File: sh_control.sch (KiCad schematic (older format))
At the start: 77 parts, among them IC1 SN75240PW, IC2 LM317MDCY, IC3 TPS73533DRBT, IC4 TLV76733DGNR, IC5 TUSB2046IBVF, IC6 TPS2044BDR, IC7 SN75240PW, J1 USB_B_Micro, J2 10129381-906001BLF, J3 10129381-906001BLF, J4 USB_A, J5 USB_A, Y1 6MHz

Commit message: finished schematic, placing parts and so on
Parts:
- added C27, C28, C29, C30: 22pF, storage:C_22pF, symbol Device:C_Small
- added C31, C32: 100uF, storage:C_100uF, symbol Device:CP_Small
- added PortC1, PortD1: USB_A, Connector_USB:USB_A_Molex_67643_Horizontal, symbol Connector:USB_A
- added R27, R28, R29, R30: 15k, storage:R_15K, symbol Device:R_Small
- R14, R15, R16, R17: value 15k -> 22; footprint storage:R_15K -> storage:R_22
- renumbered D3 to Buck_1, D4 to Buck_2, TP1 to GND1, D5 to LDO1, J4 to PortA1, J5 to PortB1, TP2 to VBUS1
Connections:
- net DM3: now also R14.2, C27.1; no longer R15.2
- net DM4: now also C28.1
- net DP3: now also R15.2, C29.1; no longer R14.2
- net DP4: now also C30.1
- net GND: now also C27.2, C28.2, C29.2, C30.2, C31.2, C32.2, PortC1.4 (GND), PortC1.5 (Shield), PortD1.4 (GND), R27.1, R28.1, R29.1, R30.1; no longer R14.1, R15.1, R16.1, R17.1
- net OUT4: now reaches IC6.10 (OUT4)
- net OUT4: now also C32.1, PortD1.1 (VBUS)
- net OUT3: now reaches IC6.11 (OUT3)
- net OUT3: now also C31.1, PortC1.1 (VBUS)
- new net DM_downstream3: PortC1.2 (D-), R14.1, R29.2
- new net DM_downstream4: PortD1.2 (D-), R16.1, R30.2
- new net DP_downstream3: PortC1.3 (D+), R15.1, R27.2
- new net DP_downstream4: PortD1.3 (D+), R17.1, R28.2
- no-connect marks 12 -> 10
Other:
- moved on the sheet: C14, C15, C16, C17, C18, C21, C22, C23, C24, C25, C26, IC5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

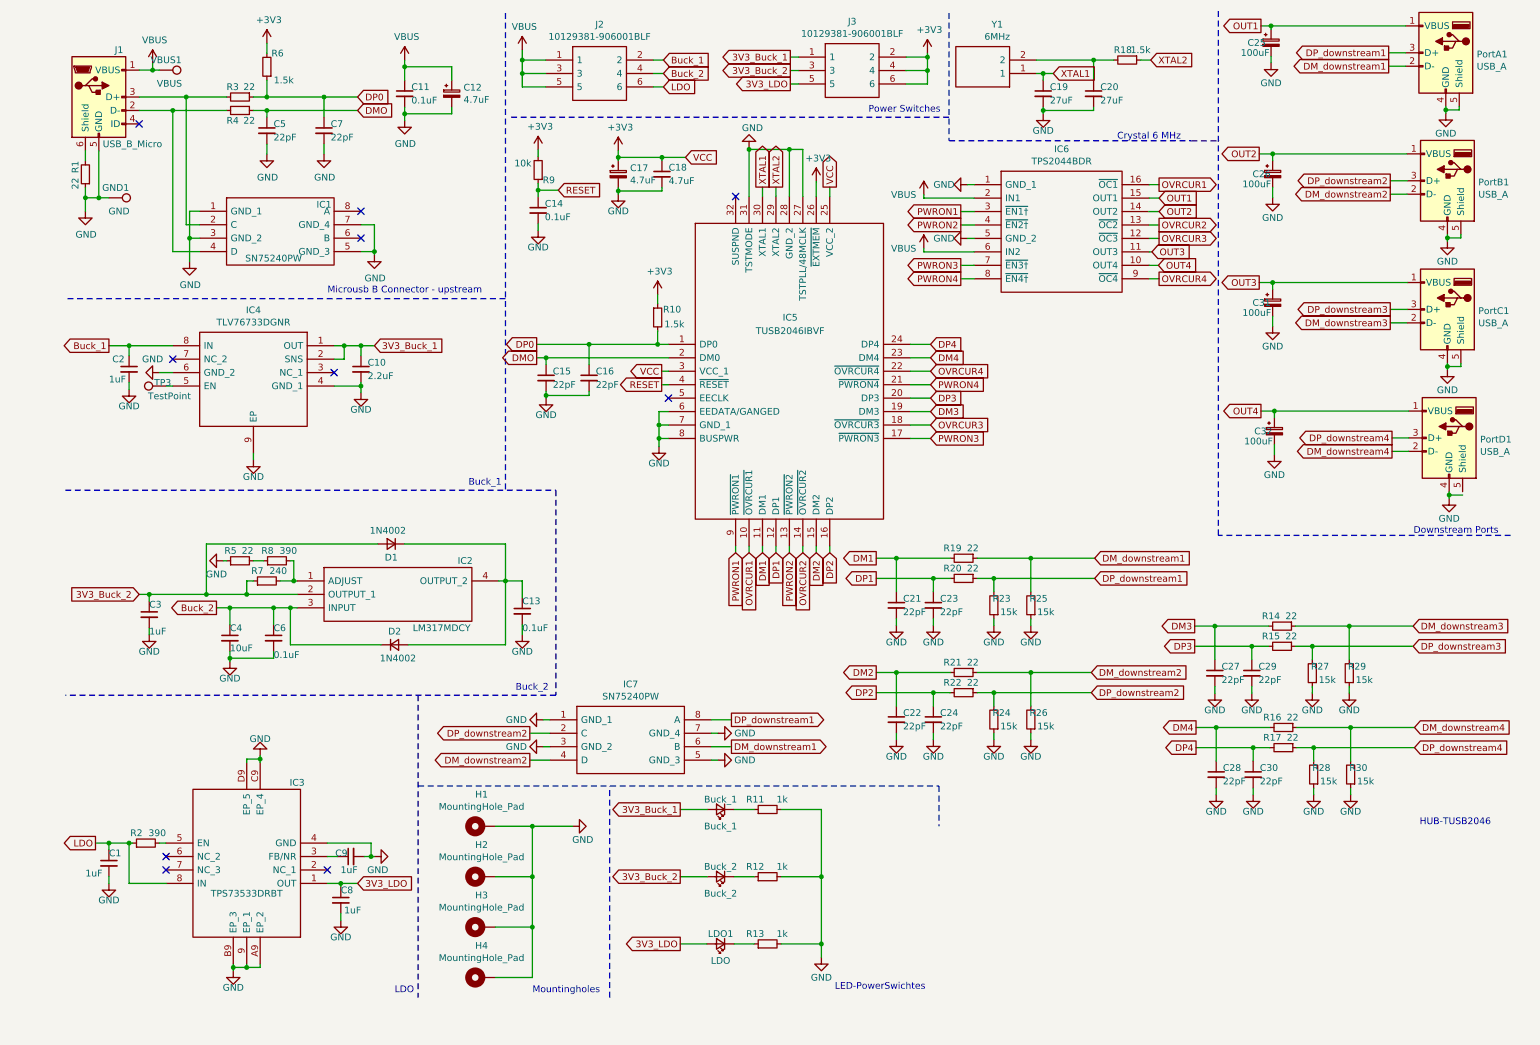
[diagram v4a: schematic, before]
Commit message: finished hub, added reste button
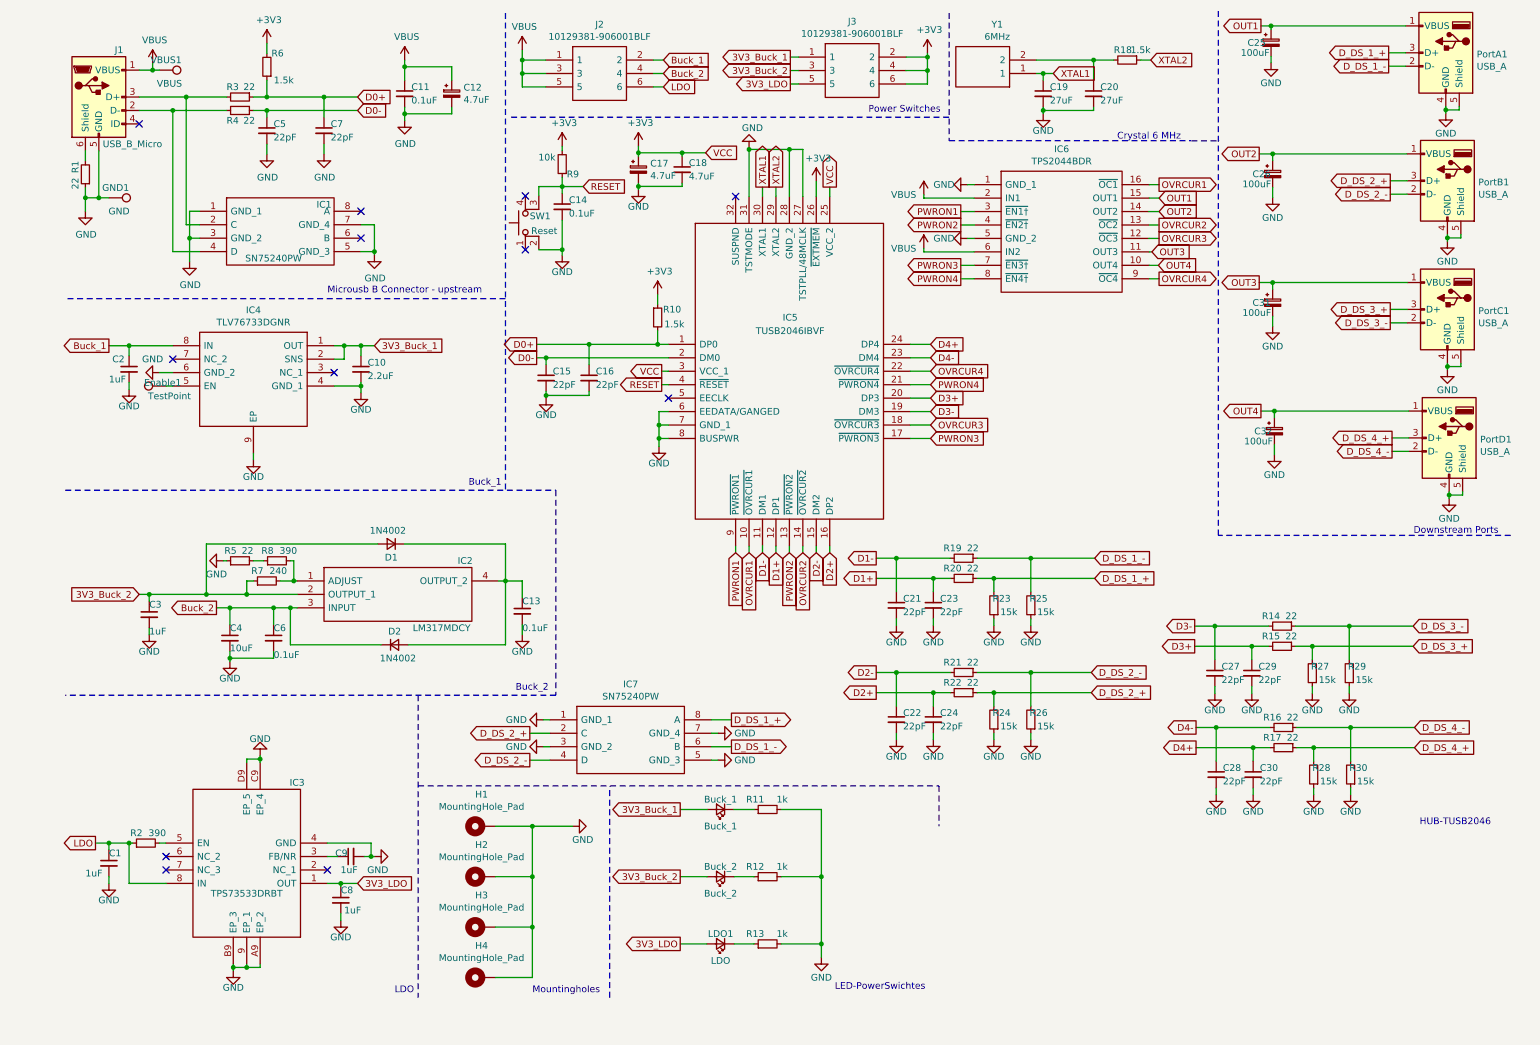
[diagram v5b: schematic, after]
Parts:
- added SW1: Reset, SamacSys_Parts:FSM4JH, symbol Switch:SW_MEC_5E
- renumbered TP3 to Enable1
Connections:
- net GND: now also PortD1.5 (Shield), SW1.2
- net RESET: now also SW1.3 (K)
- net DM1 renamed D1-
- net DM2 renamed D2-
- net DM3 renamed D3-
- net DM4 renamed D4-
- net DMO renamed D0-
- net DM_downstream1 renamed D_DS_1_-
- net DM_downstream2 renamed D_DS_2_-
- net DM_downstream3 renamed D_DS_3_-
- net DM_downstream4 renamed D_DS_4_-
- net DP0 renamed D0+
- net DP1 renamed D1+
- net DP2 renamed D2+
- net DP3 renamed D3+
- net DP4 renamed D4+
- net DP_downstream1 renamed D_DS_1_+
- net DP_downstream2 renamed D_DS_2_+
- net DP_downstream3 renamed D_DS_3_+
- net DP_downstream4 renamed D_DS_4_+
- no-connect marks 10 -> 12
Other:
- moved on the sheet: C14, C17, C18, R9

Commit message: start V3.3
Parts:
- removed Buck_1: Buck_1, SamacSys_Parts:LEDC3214X78N, symbol Device:LED_Small
- removed Buck_2: Buck_2, SamacSys_Parts:LEDC3214X78N, symbol Device:LED_Small
- removed C1, C2, C8, C9: 1uF, storage:C_1uF, symbol Device:C_Small
- removed C10: 2.2uF, storage:C_2.2F, symbol Device:C_Small
- removed C11, C14: 0.1uF, storage:C_0.1uF, symbol Device:C_Small
- removed C12, C17: 4.7uF, storage:C_4.7uF, symbol Device:CP_Small
- removed C15, C16, C21, C22, C23, C24, C27, C28, C29, C30, C5, C7: 22pF, storage:C_22pF, symbol Device:C_Small
- removed C18: 4.7uF, storage:C_4.7uF, symbol Device:C_Small
- removed C19, C20: 27uF, storage:C_27pF, symbol Device:C_Small
- removed C25, C26, C31, C32: 100uF, storage:C_100uF, symbol Device:CP_Small
- removed Enable1: TestPoint, TestPoint:TestPoint_Pad_D2.5mm, symbol Connector:TestPoint
- removed GND1: GND, TestPoint:TestPoint_Pad_D2.5mm, symbol Connector:TestPoint
- removed IC1, IC7: SN75240PW, SamacSys_Parts:SOP65P640X120-8N, symbol SamacSys_Parts:SN75240PW
- removed IC3: TPS73533DRBT, SamacSys_Parts:TPS73533DRBT, symbol SamacSys_Parts:TPS73533DRBT
- removed IC4: TLV76733DGNR, SamacSys_Parts:SOP65P490X110-9N, symbol SamacSys_Parts:TLV76733DGNR
- removed IC5: TUSB2046IBVF, SamacSys_Parts:QFP80P900X900X160-32N, symbol SamacSys_Parts:TUSB2046IBVF
- removed IC6: TPS2044BDR, SamacSys_Parts:SOIC127P600X175-16N, symbol SamacSys_Parts:TPS2044BDR
- removed J1: USB_B_Micro, Connector_USB:USB_Micro-B_Molex-105017-0001, symbol Connector:USB_B_Micro
- removed J2, J3: 10129381-906001BLF, SamacSys_Parts:HDRV6W67P254_2X3_762X483X858P, symbol SamacSys_Parts:10129381-906001BLF
- removed LDO1: LDO, SamacSys_Parts:LEDC3214X78N, symbol Device:LED_Small
- removed PortA1, PortB1, PortC1, PortD1: USB_A, Connector_USB:USB_A_Molex_67643_Horizontal, symbol Connector:USB_A
- removed R1, R14, R15, R16, R17, R19, R20, R21, R22, R3, R4: 22, storage:R_22, symbol Device:R_Small
- removed R10, R18, R6: 1.5k, storage:R_1K5, symbol Device:R_Small
- removed R11, R12, R13: 1k, storage:R_1K, symbol Device:R_Small
- removed R2: 390, storage:R_390, symbol Device:R_Small
- removed R23, R24, R25, R26, R27, R28, R29, R30: 15k, storage:R_15K, symbol Device:R_Small
- removed R9: 10k, storage:R_10K, symbol Device:R_Small
- removed SW1: Reset, SamacSys_Parts:FSM4JH, symbol Switch:SW_MEC_5E
- removed VBUS1: VBUS, TestPoint:TestPoint_Pad_D2.5mm, symbol Connector:TestPoint
- removed Y1: 6MHz, SamacSys_Parts:LFXTAL036567BULK, symbol SamacSys_Parts:LFXTAL036567BULK
- added IC2: TUSB8041IPAPRQ1, QFP50P1200X1200X120-65N, symbol SamacSys_Parts:TUSB8041IPAPRQ1
- added J1: 692221030100, WR-COM_USB_TYPE_B, symbol SamacSys_Parts:692221030100
- added J? (x4): 692121030100, 692121030100, symbol SamacSys_Parts:692121030100
- renumbered C3 to C1, C4 to C2, C6 to C3, C13 to C4, IC2 to IC1, R5 to R1, R7 to R2, R8 to R3
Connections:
- net labels removed: +3V3, 3V3_Buck_1, 3V3_Buck_2, 3V3_LDO, Buck_1, Buck_2, D0+, D0-, D1+, D1-, D2+, D2-, D3+, D3-, D4+, D4-, D_DS_1_+, D_DS_1_-, D_DS_2_+, D_DS_2_-, D_DS_3_+, D_DS_3_-, D_DS_4_+, D_DS_4_-, LDO, OUT1, OUT2, OUT3, OUT4, OVRCUR1, OVRCUR2, OVRCUR3, OVRCUR4, PWRON1, PWRON2, PWRON3, PWRON4, RESET, VBUS, VCC, XTAL1, XTAL2
- wire segments 367 -> 44
- no-connect marks 12 -> 0
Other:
- note removed: "Buck_1\n"
- note removed: "Buck_2\n"
- note removed: "Crystal 6 MHz"
- note removed: "Downstream Ports"
- note removed: "Microusb B Connector - upstream\n\n"
- note removed: "Power Switches"
- moved on the sheet: C1, C2, C3, C4, D1, D2, H1, H2, H3, H4, IC1, R1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

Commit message: orderd
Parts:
- removed D1, D2: 1N4002, storage:D_1N4002, symbol Device:D_Small
- removed IC1: LM317MDCY, SamacSys_Parts:SOT230P700X180-4N, symbol SamacSys_Parts:LM317MDCY
- removed IC2: TUSB8041IPAPRQ1, QFP50P1200X1200X120-65N, symbol SamacSys_Parts:TUSB8041IPAPRQ1
- removed J1: 692221030100, WR-COM_USB_TYPE_B, symbol SamacSys_Parts:692221030100
- removed J? (x4): 692121030100, 692121030100, symbol SamacSys_Parts:692121030100
- added BR1, BR2, BR3, BR4, BR5: Bridge, SamacSys_Parts:SOP510P1005X330-4N, symbol SamacSys_Parts:DF08SA-E3_77
- added C10, C11: 18pF, Capacitor_SMD:C_0603_1608Metric, symbol Device:C_Small
- added C12, C13, C14, C15, C18, C19, C20, C25, C29, C31, C5, C6, C7, C8: 0.1uF, Capacitor_SMD:C_0402_1005Metric, symbol Device:C_Small
- added C16, C17, C22, C24, C28, C30: 1nF, Capacitor_SMD:C_0603_1608Metric, symbol Device:C_Small
- added C21, C23, C26, C27: 100uF, SamacSys_Parts:CAPPRD350W52D800H1300, symbol SamacSys_Parts:860010674014
- added C9: 4.7uF, Capacitor_SMD:C_1206_3216Metric, symbol Device:C_Small
- added D1: PWR, LED_SMD:LED_0402_1005Metric, symbol Device:LED_Small
- added D2: PWR1, LED_SMD:LED_0402_1005Metric, symbol Device:LED_Small
- added D3: PWR2, LED_SMD:LED_0402_1005Metric, symbol Device:LED_Small
- added D4: PWR3, LED_SMD:LED_0402_1005Metric, symbol Device:LED_Small
- added D5: PWR4, LED_SMD:LED_0402_1005Metric, symbol Device:LED_Small
- added IC1: TLV76733DGNR, SamacSys_Parts:SOP65P490X110-9N, symbol SamacSys_Parts:TLV76733DGNR
- added IC2: TPS2044BDR, SamacSys_Parts:SOIC127P600X175-16N, symbol SamacSys_Parts:TPS2044BDR
- added J1: USB_B_Micro, Connector_USB:USB_Micro-B_Molex-105017-0001, symbol Connector:USB_B_Micro
- added J2, J3, J4, J5: 67643-0910, SamacSys_Parts:676430910, symbol SamacSys_Parts:67643-0910
- added R10, R11, R4, R6, R7, R9: 100K, Resistor_SMD:R_0402_1005Metric, symbol Device:R_Small
- added R12, R13, R14, R15: 4.7K, Resistor_SMD:R_1206_3216Metric, symbol Device:R_Small
- added R5: 100K, Resistor_SMD:R_1206_3216Metric, symbol Device:R_Small
- added R8: 330, Resistor_SMD:R_0603_1608Metric, symbol Device:R_Small
- added U1: USB2514B_Bi, Package_DFN_QFN:QFN-36-1EP_6x6mm_P0.5mm_EP3.7x3.7mm, symbol Interface_USB:USB2514B_Bi
- added Y1: 24MHz 10ppm, Crystal:Crystal_SMD_2016-4Pin_2.0x1.6mm, symbol Device:Crystal_GND24
- C1: footprint storage:C_1uF -> Capacitor_SMD:C_0805_2012Metric
- C2: value 10uF -> 2.2uF; footprint storage:C_10uF -> Capacitor_SMD:C_0603_1608Metric
- C3, C4: footprint storage:C_0.1uF -> Capacitor_SMD:C_0402_1005Metric
- R1: value 22 -> 100K; footprint storage:R_22 -> Resistor_SMD:R_0402_1005Metric
- R2: value 240 -> 4.7K; footprint storage:R_240 -> Resistor_SMD:R_1206_3216Metric
- R3: value 390 -> 1Meg; footprint storage:R_390 -> Resistor_SMD:R_0805_2012Metric
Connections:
- net labels added: +3V3, +5V, 3V3, HS_IND, LOCAL_PWR, OCS_N1, OCS_N2, OCS_N3, OCS_N4, PRTPWR1, PRTPWR2, PRTPWR3, PRTPWR4, PWR1, PWR2, PWR3, PWR4, USBDN_1+, USBDN_1-, USBDN_2+, USBDN_2-, USBDN_3+, USBDN_3-, USBDN_4+, USBDN_4-, USBUP_+, USBUP_-, VBUS_DET, VBUS_UP, VSS, XTALIN, XTALOUT
- wire segments 44 -> 271
- no-connect marks 0 -> 4
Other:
- note removed: "HUB-TUSB2046"
- note removed: "LDO"
- note removed: "LED-PowerSwichtes"
- moved on the sheet: H1, H2, H3, H4
